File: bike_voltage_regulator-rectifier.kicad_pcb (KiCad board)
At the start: 2 copper layers, 32.1 x 50 mm, 25 parts, among them U1 GBU1510_C22447862, U2 IRFB4110PBF, U3 MBR2045CT_C173461, U4 LM2903DRG4, U5 TL431_C181103, U6 MMBT3904, U7 MMBT3906LT1G, U8 436500400

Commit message: backup
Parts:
- added G***: LOGO, LOGO, B.Cu at (165.3, 107.7)
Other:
- board text added: "- + AC AC"
- board text added: "Regulator-Rectifier PROTOYPE, NOT FOR RESALE NO REGULATORY APPROVAL USE AT OWN RISK EVALUATION ONLY DESIGNED BY INDOOR_INDUSTRY 10/2026"

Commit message: first prototype
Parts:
- U8: moved to B.Cu
- moved U8 0.08 mm to (157.1, 77.5), turned to 0 degrees
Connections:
- U8 pad 1: AC1 -> VOUT
- U8 pad 2: AC2 -> GND
- U8 pad 3: VOUT -> AC2
- U8 pad 4: GND -> AC1
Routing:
- net VOUT: track 134.8 -> 131.6 mm, vias 0 -> 1
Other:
- board text added: "+ - AC AC"
- board text added: "AC AC - +"
- board text removed: "- + AC AC"
- board text removed: "AC AC + -"

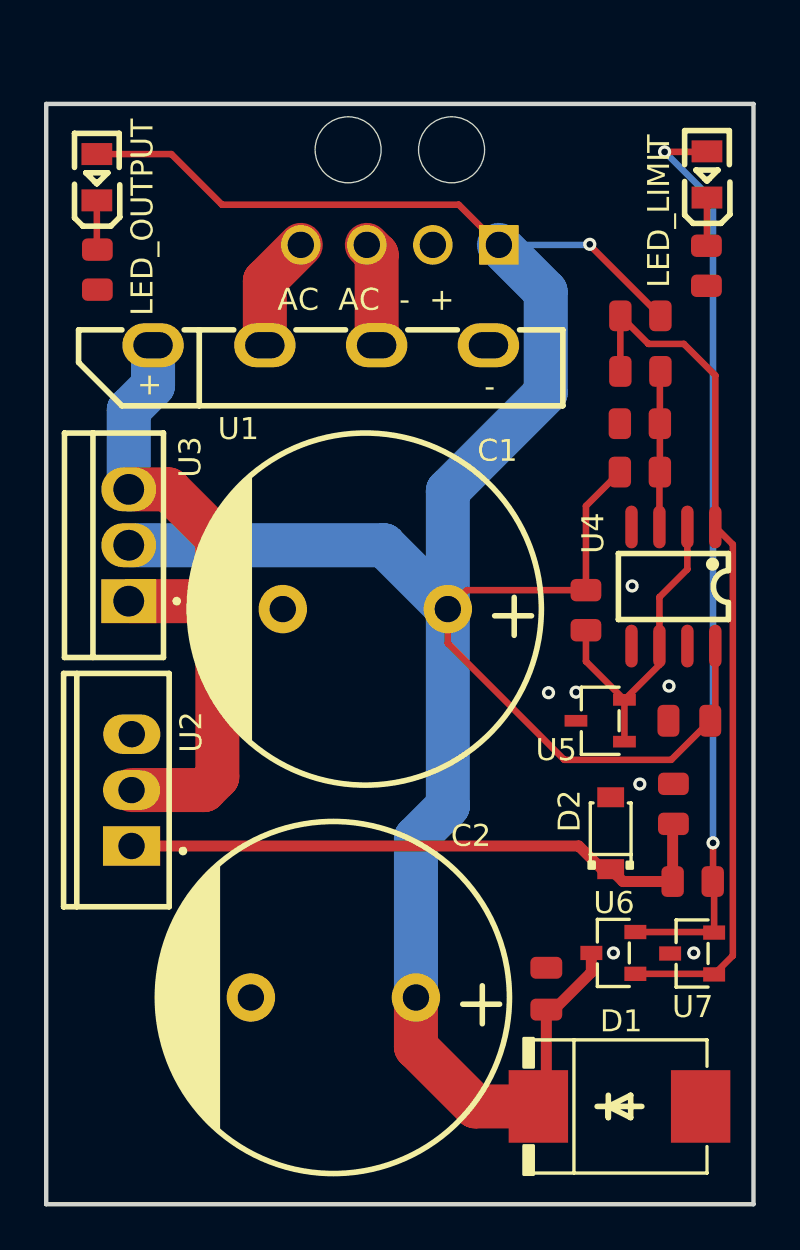
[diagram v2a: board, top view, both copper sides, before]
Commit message: Changed rectification architecture
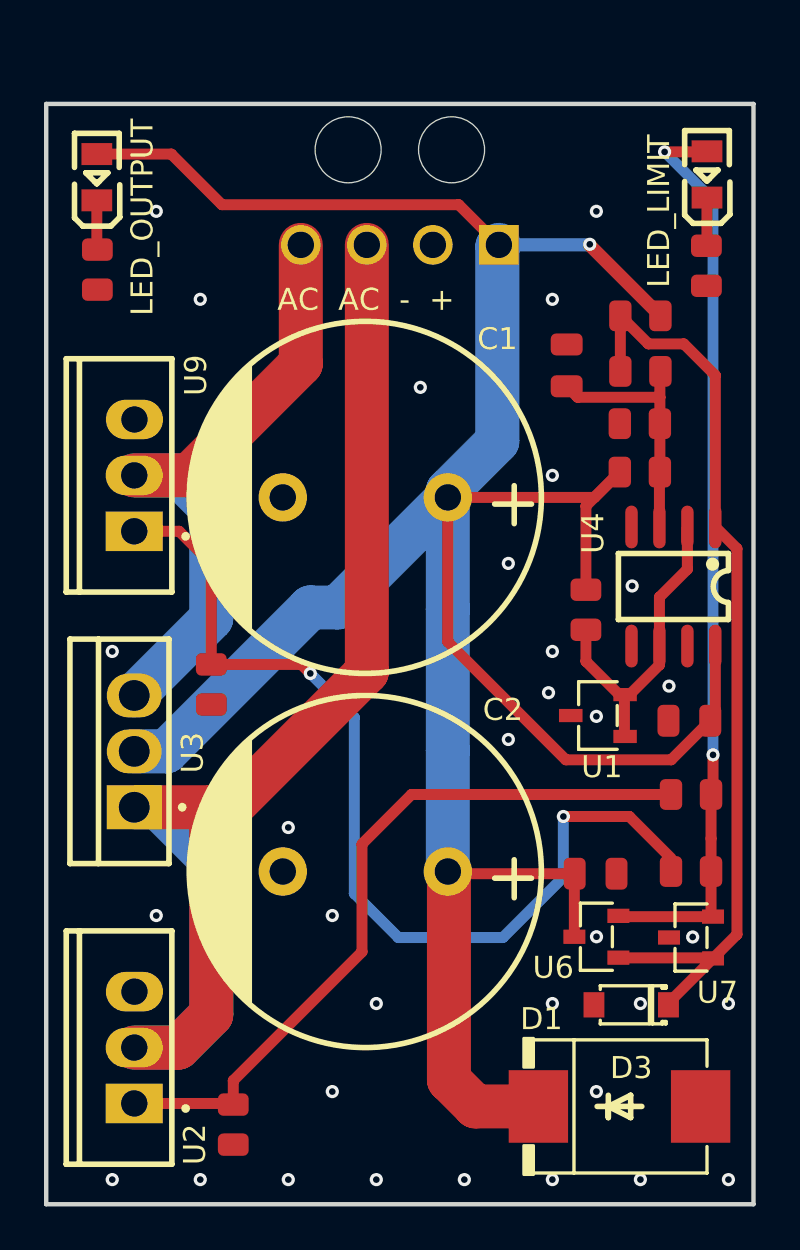
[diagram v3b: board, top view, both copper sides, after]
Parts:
- removed D2: BZT52C15, regulator_library:SOD-123_L2.7-W1.6-LS3.7-RD
- removed R5: 2.2kΩ, PCM_JLCPCB:R_0805
- removed U5: TL431_C181103, regulator_library:SOT-23-3_L3.0-W1.7-P0.95-LS2.9-BR
- added C5: 22nF, PCM_JLCPCB:C_0805, F.Cu at (164.7, 83.0)
- added D3: BZT52C16-TP, regulator_library:SOD-123_L2.8-W1.8-LS3.7-RD, F.Cu at (167.6, 112.1)
- added R1: 3.3kΩ, PCM_JLCPCB:R_0805, F.Cu at (165.5, 94.1)
- added R13: 10Ω, PCM_JLCPCB:R_0805, F.Cu at (170.3, 106.0)
- added R4: 10kΩ, PCM_JLCPCB:R_0805, F.Cu at (148.5, 97.5)
- added U9: IRFB4110PBF, regulator_library:TO-220-3_L10.0-W4.5-P2.54-L, F.Cu at (145.0, 88.0)
- U1: value GBU1510_C22447862 -> TL431BQDBZR; footprint regulator_library:GBU_4P-L22.0-W3.5-P5.08_GBU808 -> regulator_library:SOT-23-3_L2.9-W1.6-P1.90-LS2.8-BR
- moved R3 24.7 mm to (149.5, 117.5), turned to -90 degrees
- moved U1 21.0 mm to (166.1, 98.9), turned to 0 degrees
- moved U2 11.7 mm to (145.0, 114.0)
- moved U3 9.37 mm to (145.0, 100.5)
- moved C2 5.91 mm to (155.5, 106.0)
- moved C4 5.68 mm to (166.0, 106.1), turned to 0 degrees
- moved C1 5.08 mm to (155.5, 89.0)
- moved R7 3.96 mm to (170.3, 102.5)
- moved U6 1.06 mm to (166.0, 109.0)
- moved U7 0.73 mm to (170.3, 109.0)
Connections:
- net GATE renamed GATE_1
- U1 pad 1: /VRAW -> REF
- U1 pad 2: AC1 -> REF
- U1 pad 3: AC2 -> GND
- U2 pad 2: /VRAW -> AC1
- U3 pad 1: /VRAW -> AC1
- U3 pad 3: /VRAW -> AC2
- U8 pad 3: AC2 -> AC1
- U8 pad 4: AC1 -> AC2
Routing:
- net AC1: track 5.24 -> 61.7 mm
- net GATE_2: track 0.00 -> 44.7 mm, vias 0 -> 2
- net /VRAW: track 31.3 -> 0.00 mm
- net AC2: track 4.75 -> 29.1 mm
- net VOUT: track 131.6 -> 139.5 mm
- net GATE_1: track 27.9 -> 33.7 mm
- net /SENSE: track 7.38 -> 11.8 mm
- net /CMP: track 39.7 -> 42.8 mm
- net GND: vias 7 -> 33
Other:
- board text added: "{ "ViaStitcher": "0.3.4", "gnd": { "HSpacing": "4", "VSpacing": "4", "HOffset": "0", "VOffset": "0", "Clearance": "0", "FillStyle": "Stagger", "RequireAllCopperLayers": false, "AdaptiveFill": false, "MinSpacingPercent": "80", "MaxSpacingPercent": "150" } }"
